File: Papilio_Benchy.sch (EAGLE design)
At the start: 133 parts, among them IC1 FT2232H, J1 USB MICRO, J4 HDMI-TYPE-A-RECEPTICALFCI1002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, SW1 SWITCH-2CH-6P-3010010P1, SW2 EVQQ2, T1 MOSFET-NCHANNELSMD, U1 ATMEGA32U4-XUMU, U11 PCA9306, U2 LTC3419EMS, U3 93C46B, U5 ARDUINO_MEGA_SHIELD, X2 12MHz, Y1 16MHz KX-7

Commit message: Power Supply PAR'd
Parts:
- removed PWR: (no value), led:LEDCHIP-LED0805
- removed R5: 1K8, GadgetFactory:R0805
- added PWRSELECT: (no value), jumper:JP2E
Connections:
- removed net 5V: C49.2, CONN1USB.VUSB, R11.2, R32A.2, U2.MODE, U2.RUN1, U2.VIN
- removed net N$1: PWR.A, R5A.1
- new net VBUS_A: CONN1USB.VUSB, PWRSELECT.1
- net 5V0: now also C49.2, PWRSELECT.2, R11.2, R32A.2, U2.MODE, U2.RUN1, U2.VIN; no longer R5A.2
- net GND: no longer PWR.C
- net VI: now also PWRSELECT.3
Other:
- moved on the sheet: S6BNA, S6BVCCAUX, S6BVCCINT

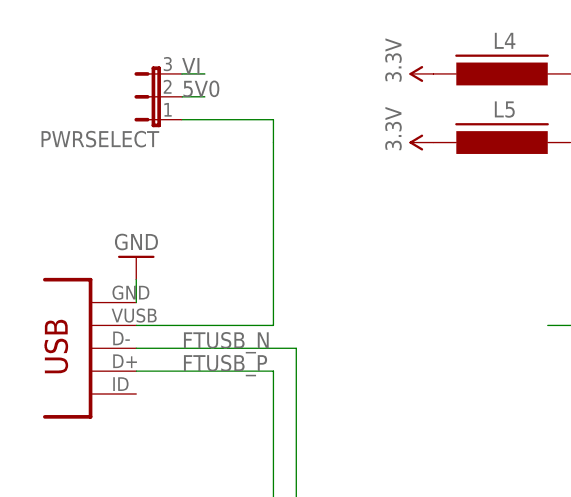
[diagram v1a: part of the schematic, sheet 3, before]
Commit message: SRAM Cleaned up
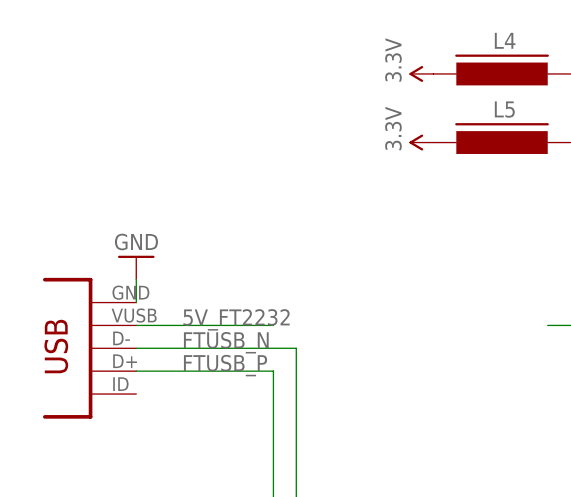
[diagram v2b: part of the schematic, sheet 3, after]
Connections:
- net VBUS_A renamed 5V_FT2232
- net XUSB renamed 5V_ARDUINO
- net 5V0: now also PWRIN.1
- net VI: no longer PWRIN.1
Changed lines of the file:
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@@
 </instance>
 <instance part="PWRIN" gate="A" x="193.04" y="444.5" rot="R270"/>
+<instance part="PWRSELECT" gate="1" x="162.56" y="472.44" rot="R90"/>
 </instances>
 <busses>
@@
 <pinref part="R32" gate="A" pin="2"/>
 </segment>
-</net>
-<net name="VI" class="0">
+<segment>
+<wire x1="165.1" y1="472.44" x2="167.64" y2="472.44" width="0.2032" layer="91"/>
+<label x="165.1" y="472.44" size="1.778" layer="95"/>
+<pinref part="PWRSELECT" gate="1" pin="2"/>
+</segment>
 <segment>
 <wire x1="170.18" y1="444.5" x2="190.5" y2="444.5" width="0.2032" layer="91"/>
 <label x="172.72" y="444.5" size="1.778" layer="95"/>
 <pinref part="PWRIN" gate="A" pin="1"/>
+</segment>
+</net>
+<net name="VI" class="0">
+<segment>
+<wire x1="165.1" y1="474.98" x2="167.64" y2="474.98" width="0.2032" layer="91"/>
+<label x="165.1" y="474.98" size="1.778" layer="95"/>
+<pinref part="PWRSELECT" gate="1" pin="3"/>
 </segment>
 </net>
@@
 <pinref part="R32" gate="A" pin="1"/>
 <pinref part="PWR1" gate="G$1" pin="A"/>
+</segment>
+</net>
+<net name="5V_FT2232" class="0">
+<segment>
+<wire x1="165.1" y1="469.9" x2="175.26" y2="469.9" width="0.2032" layer="91"/>
+<pinref part="PWRSELECT" gate="1" pin="1"/>
 </segment>
 </net>
@@
 <instance part="CONN1" gate="USB" x="12.7" y="142.24"/>
 <instance part="U3" gate="1" x="45.72" y="73.66" rot="MR0"/>
-<instance part="PWRSELECT" gate="1" x="20.32" y="170.18" rot="R90"/>
 </instances>
 <busses>
@@
 </segment>
 </net>
-<net name="VI" class="0">
-<segment>
-<wire x1="22.86" y1="172.72" x2="25.4" y2="172.72" width="0.2032" layer="91"/>
-<label x="22.86" y="172.72" size="1.778" layer="95"/>
-<pinref part="PWRSELECT" gate="1" pin="3"/>
-</segment>
-</net>
-<net name="VBUS_A" class="0">
-<segment>
-<wire x1="33.02" y1="154.94" x2="33.02" y2="144.78" width="0.2032" layer="91"/>
-<wire x1="33.02" y1="165.1" x2="33.02" y2="154.94" width="0.1524" layer="91"/>
-<wire x1="22.86" y1="167.64" x2="33.02" y2="167.64" width="0.2032" layer="91"/>
-<wire x1="33.02" y1="167.64" x2="33.02" y2="165.1" width="0.2032" layer="91"/>
-<pinref part="PWRSELECT" gate="1" pin="1"/>
+<net name="5V_FT2232" class="0">
+<segment>
 <pinref part="CONN1" gate="USB" pin="VUSB"/>
 <wire x1="17.78" y1="144.78" x2="33.02" y2="144.78" width="0.1524" layer="91"/>
-</segment>
-</net>
-<net name="5V0" class="0">
-<segment>
-<wire x1="22.86" y1="170.18" x2="25.4" y2="170.18" width="0.2032" layer="91"/>
-<label x="22.86" y="170.18" size="1.778" layer="95"/>
-<pinref part="PWRSELECT" gate="1" pin="2"/>
+<label x="22.86" y="144.78" size="1.778" layer="95"/>
 </segment>
 </net>
@@
 </segment>
 </net>
-<net name="XUSB" class="3">
-<segment>
-<wire x1="-81.28" y1="0" x2="-81.28" y2="10.16" width="0.1524" layer="91"/>
-<wire x1="-81.28" y1="10.16" x2="-66.04" y2="10.16" width="0.1524" layer="91"/>
+<net name="5V_ARDUINO" class="3">
+<segment>
 <wire x1="-101.6" y1="0" x2="-81.28" y2="0" width="0.1524" layer="91"/>
-<label x="-91.44" y="0" size="1.778" layer="95" rot="MR0"/>
-<label x="-78.74" y="10.16" size="1.778" layer="95"/>
+<label x="-81.28" y="0" size="1.778" layer="95" rot="MR0"/>
 <pinref part="J1" gate="G$1" pin="VBUS"/>
 </segment>

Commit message: Before connecting Avr JTAG
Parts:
- removed D2: CD1206-S01575, diode:DIODE-MINIMELF
- removed R47, R48, R49: 390, GadgetFactory:R0603
- removed R7: 10K, GadgetFactory_6.0:R0805
- C11, C3, C4, C5, C6, C7, C9: device SmartPrj:C-EUC0603 -> SmartPrj:C-EUC0603K
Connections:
- removed net +5V: C3.1, C4.1, D2.C, L6.1, R7A.2, RN2A.1, RN2C.1, RN2D.1, U1.UVCC, U1.VCC, U1.VCC1
- removed net N$10: R49A.2, U1.(SCLK/PCINT1)PB1
- removed net N$11: R48A.2, U1.(PDI/MOSI/PCINT2)PB2
- removed net N$12: R47A.2, U1.(PD0/MISO/PCINT3)PB3
- removed net VI: PWRSELECT.3
- net 5V0: now also C3.1, C4.1, L6.1, RN2A.1, RN2C.1, RN2D.1, U1.RESET, U1.UVCC, U1.VCC, U1.VCC1
- net 5V_ARDUINO: now also PWRSELECT.3
- net ARD_RESET: no longer D2.A, R7A.1, U1.RESET
- net MEGA_D40: no longer R47A.1
- net MEGA_D41: no longer R48A.1
- net MEGA_D42: no longer R49A.1

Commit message: Fully routed except for HDMI and AVR JTAG
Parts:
- removed LED1: (no value), led:LEDCHIPLED_0805
- removed ON: Green, led:LEDCHIPLED_0805
- removed R37: 390, GadgetFactory:R0805
- removed RN2: 1K, resistor-dil:4R-NCAY16
- removed RX, TX: Yellow, led:LEDCHIPLED_0805
- R2: value NM -> 10K; device SmartPrj:R-EU_R0402 -> GadgetFactory_6.0:R0603
- R3: value NM -> 1K; device SmartPrj:R-EU_R0402 -> GadgetFactory_6.0:R0603
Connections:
- net RD+ renamed AVRUSB_P
- net RD- renamed AVRUSB_N
- removed net ATMEGA_D2/SDA: R14A.2, U1.(SDA/INT1)PD1, U5.*D2
- removed net ATMEGA_D3/SCL: R15A.2, U1.(OC0B/SCL/INT0)PD0, U5.*D3
- removed net N$3: ON.A, RN2A.2
- removed net N$4: RN2C.2, TX.A
- removed net N$5: RN2D.2, RX.A
- removed net N$7: LED1.A, R37A.1
- removed net UGND: C7.2, R3.2, U1.UGND
- removed net VUSB: U1.VBUS
- new net ATMEGA_D2: R14A.2, U1.(PCINT5/OC1A/#OC4B/ADC12)PB5, U5.*D2
- new net ATMEGA_D3: R15A.2, U1.(ADC11/PCINT4)PB4, U5.*D3
- net 3V3: now also C3.1, C4.1, L6.1, R2A.2, U1.UVCC, U1.VCC, U1.VCC1
- net 5V0: no longer C3.1, C4.1, L6.1, RN2A.1, RN2C.1, RN2D.1, U1.RESET, U1.UVCC, U1.VCC, U1.VCC1
- net AGND: no longer C6.1, R2.1
- net ARD_RESET: now also R2A.1, U1.RESET
- net AREF: now also U5.AREF
- net ATMEGA_D4: now also U1.(T0/OC4D/ADC10)PD7; no longer U1.(OC3A/#0C4A)PC6
- net ATMEGA_D5*: now also U1.(T1/#OC4D/ADC9)PD6; no longer U1.(PCINT6/OC1B/OC4B/ADC13)PB6
- net ATMEGA_D6*: now also U1.(ICP1/ADC8)PD4; no longer U1.(PCINT5/OC1A/#OC4B/ADC12)PB5
- net ATMEGA_D7: now also U1.(SDA/INT1)PD1; no longer U1.(ADC11/PCINT4)PB4
- net ATMEGA_IO10*: now also U1.(PD0/MISO/PCINT3)PB3; no longer U1.(ICP1/ADC8)PD4
- net ATMEGA_IO11*: now also U1.(PDI/MOSI/PCINT2)PB2; no longer U1.(PCINT7/OC0A/OC1C/#RTS)PB7
- net ATMEGA_IO12: now also U1.(SCLK/PCINT1)PB1; no longer U1.(INT6/AIN0)PE6
- net ATMEGA_IO13*: now also R3A.2, U1.(INT6/AIN0)PE6; no longer RN2B.1, U1.(ICP3/CLK0/OC4A)PC7
- net ATMEGA_IO8: now also U1.(OC0B/SCL/INT0)PD0; no longer U1.(T0/OC4D/ADC10)PD7
- net ATMEGA_IO9*: now also U1.(PCINT7/OC0A/OC1C/#RTS)PB7; no longer U1.(T1/#OC4D/ADC9)PD6
- net ATMEGA_RXLED: no longer RX.C
- net ATMEGA_TXLED: no longer TX.C
- net GND: now also C6.1, C7.2, U1.UGND; no longer LED1.C, ON.C, R2.2, R3.1
- net MEGA_D14: now also U1.(PCINT6/OC1B/OC4B/ADC13)PB6
- net MEGA_D15: now also U1.(OC3A/#0C4A)PC6
- net MEGA_D16: now also U1.(ICP3/CLK0/OC4A)PC7
- net MEGA_D17: no longer R37A.2
- net N$2: now also R3A.1; no longer RN2B.2
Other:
- moved on the sheet: L

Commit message: Fully placed and routed! Needs verification and cleanup.
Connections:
- removed net ATMEGA_A2: U1.(ADC4/TCK)PF4, U5.A2
- removed net ATMEGA_A3: U1.(ADC5/TMS)PF5, U5.A3
- removed net ATMEGA_A4: U1.(ADC6/TDO)PF6, U5.A4
- removed net ATMEGA_A5: U1.(ADC7/TDI)PF7, U5.A5
- removed net MEGA_D28: S6B1.IO_L42P_GCLK7_1, U5.D28
- removed net MEGA_D30: S6B1.IO_L43P_GCLK5_1, U5.D30
- removed net MEGA_D32: S6B1.IO_L45P_1, U5.D32
- removed net MEGA_D34: S6B1.IO_L46P_1, U5.D34
- new net MEGA_D28/A5: S6B1.IO_L42P_GCLK7_1, U1.(ADC7/TDI)PF7, U5.A5, U5.D28
- new net MEGA_D30/A4: S6B1.IO_L43P_GCLK5_1, U1.(ADC6/TDO)PF6, U5.A4, U5.D30
- new net MEGA_D32/A3: S6B1.IO_L45P_1, U1.(ADC5/TMS)PF5, U5.A3, U5.D32
- new net MEGA_D34/A2: S6B1.IO_L46P_1, U1.(ADC4/TCK)PF4, U5.A2, U5.D34
- net MEGA_D49: now also J4.DATA0+; no longer J4.CLOCK+
- net MEGA_D50: now also J4.DATA0-; no longer J4.CLOCK-
- net MEGA_D51: now also J4.CLOCK+; no longer J4.DATA0+
- net MEGA_D52: now also J4.CLOCK-; no longer J4.DATA0-
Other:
- note removed: "TODO: Reset Line... Protect FPGA if 5V."
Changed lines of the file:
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@@
 <setting verticaltext="up"/>
 </settings>
-<grid distance="0.05" unitdist="inch" unit="inch" style="lines" multiple="1" display="no" altdistance="0.025" altunitdist="inch" altunit="inch"/>
+<grid distance="0.1" unitdist="inch" unit="inch" style="lines" multiple="1" display="no" altdistance="0.01" altunitdist="inch" altunit="inch"/>
 <layers>
 <layer number="1" name="Top" color="4" fill="1" visible="no" active="no"/>
@@
 </segment>
 </net>
-<net name="MEGA_D28" class="0">
+<net name="MEGA_D28/A5" class="0">
 <segment>
 <wire x1="10.16" y1="58.42" x2="-20.32" y2="58.42" width="0.1524" layer="91"/>
@@
 <pinref part="S6" gate="B1" pin="IO_L42P_GCLK7_1"/>
 </segment>
+<segment>
+<wire x1="-68.58" y1="124.46" x2="-45.72" y2="124.46" width="0.1524" layer="91"/>
+<label x="-63.5" y="124.46" size="1.778" layer="95"/>
+<pinref part="U5" gate="ARDUINO_MEGA" pin="A5"/>
+</segment>
 </net>
 <net name="MEGA_D29" class="0">
@@
 </segment>
 </net>
-<net name="MEGA_D30" class="0">
+<net name="MEGA_D30/A4" class="0">
 <segment>
 <wire x1="10.16" y1="53.34" x2="-20.32" y2="53.34" width="0.1524" layer="91"/>
@@
 <pinref part="S6" gate="B1" pin="IO_L43P_GCLK5_1"/>
 </segment>
+<segment>
+<wire x1="-68.58" y1="127" x2="-45.72" y2="127" width="0.1524" layer="91"/>
+<label x="-63.5" y="127" size="1.778" layer="95"/>
+<pinref part="U5" gate="ARDUINO_MEGA" pin="A4"/>
+</segment>
 </net>
 <net name="MEGA_D31" class="0">
@@
 </segment>
 </net>
-<net name="MEGA_D32" class="0">
+<net name="MEGA_D32/A3" class="0">
 <segment>
 <wire x1="10.16" y1="48.26" x2="-20.32" y2="48.26" width="0.1524" layer="91"/>
@@
 <pinref part="S6" gate="B1" pin="IO_L45P_1"/>
 </segment>
+<segment>
+<wire x1="-68.58" y1="129.54" x2="-45.72" y2="129.54" width="0.1524" layer="91"/>
+<label x="-63.5" y="129.54" size="1.778" layer="95"/>
+<pinref part="U5" gate="ARDUINO_MEGA" pin="A3"/>
+</segment>
 </net>
 <net name="MEGA_D33" class="0">
@@
 </segment>
 </net>
-<net name="MEGA_D34" class="0">
+<net name="MEGA_D34/A2" class="0">
 <segment>
 <wire x1="10.16" y1="43.18" x2="-20.32" y2="43.18" width="0.1524" layer="91"/>
@@
 <pinref part="S6" gate="B1" pin="IO_L46P_1"/>
 </segment>
+<segment>
+<wire x1="-68.58" y1="132.08" x2="-45.72" y2="132.08" width="0.1524" layer="91"/>
+<label x="-63.5" y="132.08" size="1.778" layer="95"/>
+<pinref part="U5" gate="ARDUINO_MEGA" pin="A2"/>
+</segment>
 </net>
 <net name="MEGA_D35" class="0">
@@
 </segment>
 </net>
-<net name="ATMEGA_A5" class="0">
-<segment>
-<wire x1="-68.58" y1="124.46" x2="-45.72" y2="124.46" width="0.1524" layer="91"/>
-<label x="-63.5" y="124.46" size="1.778" layer="95"/>
-<pinref part="U5" gate="ARDUINO_MEGA" pin="A5"/>
-</segment>
-</net>
-<net name="ATMEGA_A4" class="0">
-<segment>
-<wire x1="-68.58" y1="127" x2="-45.72" y2="127" width="0.1524" layer="91"/>
-<label x="-63.5" y="127" size="1.778" layer="95"/>
-<pinref part="U5" gate="ARDUINO_MEGA" pin="A4"/>
-</segment>
-</net>
-<net name="ATMEGA_A3" class="0">
-<segment>
-<wire x1="-68.58" y1="129.54" x2="-45.72" y2="129.54" width="0.1524" layer="91"/>
-<label x="-63.5" y="129.54" size="1.778" layer="95"/>
-<pinref part="U5" gate="ARDUINO_MEGA" pin="A3"/>
-</segment>
-</net>
-<net name="ATMEGA_A2" class="0">
-<segment>
-<wire x1="-68.58" y1="132.08" x2="-45.72" y2="132.08" width="0.1524" layer="91"/>
-<label x="-63.5" y="132.08" size="1.778" layer="95"/>
-<pinref part="U5" gate="ARDUINO_MEGA" pin="A2"/>
-</segment>
-</net>
 <net name="ATMEGA_A1" class="0">
 <segment>
@@
 <plain>
 <text x="-99.06" y="15.24" size="3.81" layer="94" ratio="10" rot="MR0">USB</text>
-<text x="-13.97" y="156.21" size="1.778" layer="91">TODO: Reset Line... Protect FPGA if 5V.</text>
 </plain>
 <instances>
@@
 </segment>
 </net>
-<net name="ATMEGA_A2" class="0">
+<net name="MEGA_D34/A2" class="0">
 <segment>
 <wire x1="53.34" y1="55.88" x2="71.12" y2="55.88" width="0.1524" layer="91"/>
@@
 </segment>
 </net>
-<net name="ATMEGA_A3" class="0">
+<net name="MEGA_D32/A3" class="0">
 <segment>
 <wire x1="53.34" y1="58.42" x2="71.12" y2="58.42" width="0.1524" layer="91"/>
@@
 </segment>
 </net>
-<net name="ATMEGA_A4" class="0">
+<net name="MEGA_D30/A4" class="0">
 <segment>
 <wire x1="53.34" y1="60.96" x2="71.12" y2="60.96" width="0.1524" layer="91"/>
@@
 </segment>
 </net>
-<net name="ATMEGA_A5" class="0">
+<net name="MEGA_D28/A5" class="0">
 <segment>
 <wire x1="53.34" y1="63.5" x2="71.12" y2="63.5" width="0.1524" layer="91"/>
@@
 </segment>
 </net>
-<net name="MEGA_D51" class="0">
+<net name="MEGA_D49" class="0">
 <segment>
 <wire x1="190.5" y1="137.16" x2="40.64" y2="137.16" width="0.2032" layer="91"/>
@@
 </segment>
 </net>
-<net name="MEGA_D52" class="0">
+<net name="MEGA_D50" class="0">
 <segment>
 <wire x1="190.5" y1="127" x2="40.64" y2="127" width="0.2032" layer="91"/>
@@
 </segment>
 </net>
-<net name="MEGA_D49" class="0">
-<segment>
-<wire x1="190.5" y1="121.92" x2="40.64" y2="121.92" width="0.2032" layer="91"/>
-<label x="40.64" y="121.92" size="1.778" layer="95"/>
-<pinref part="J4" gate="G$1" pin="CLOCK+"/>
-</segment>
-</net>
-<net name="MEGA_D50" class="0">
-<segment>
-<wire x1="190.5" y1="111.76" x2="40.64" y2="111.76" width="0.2032" layer="91"/>
-<label x="40.64" y="111.76" size="1.778" layer="95"/>
-<pinref part="J4" gate="G$1" pin="CLOCK-"/>
-</segment>
-</net>
 <net name="MEGA_D53" class="0">
 <segment>
@@
 </segment>
 </net>
+<net name="MEGA_D51" class="0">
+<segment>
+<wire x1="190.5" y1="121.92" x2="40.64" y2="121.92" width="0.2032" layer="91"/>
+<label x="40.64" y="121.92" size="1.778" layer="95"/>
+<pinref part="J4" gate="G$1" pin="CLOCK+"/>
+</segment>
+</net>
+<net name="MEGA_D52" class="0">
+<segment>
+<wire x1="190.5" y1="111.76" x2="40.64" y2="111.76" width="0.2032" layer="91"/>
+<label x="40.64" y="111.76" size="1.778" layer="95"/>
+<pinref part="J4" gate="G$1" pin="CLOCK-"/>
+</segment>
+</net>

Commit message: Silkscreen cleaned up.
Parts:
- removed C35, C36, C37, C38, C39, C40, C41: 0.1uF, dp_devices:CAPC603
- removed C48, C50: 22u/6V3, Bogdan_Commons:C0805
- removed C49: 10u/10V, Bogdan_Commons:C0805
- removed L5: (no value), dp_devices:FERRITE_BEAD603
- removed R33: 47K, GadgetFactory:R0805
- removed R34, R36, R38, R39: 10k, dp_devices:RESISTORR603
- removed R35: 2.2k, dp_devices:RESISTORR603
- removed R40, R41: 470, dp_devices:RESISTORR603
- removed U$9: POWER_ONLYNOTEXT, Papilio:POWER_ONLYNOTEXT
- removed U5: ARDUINO_MEGA_SHIELD, GadgetFactory_tmp:ARDUINO_MEGA_SHIELD
- added C100: 1uF, saanlima:C0402
- added C101, C102, C105: 100n, SmartPrj:C-EUC0603K
- added C103, C104: 1uF, SmartPrj:C-EUC0603K
- added C106, C107: 22p, SmartPrj:C-EUC0603K
- added C12, C13: .1uF, GadgetFactory:C0603
- added L1: 3.3uH, Bogdan_Commons:L_VLS3015
- added R100: 10K, saanlima:R0402
- added R102: 0, saanlima:R0402
- added R106, R107: 1K, saanlima:R0402
- added R109: 1M, SmartPrj:R-EU_R0603
- added R110: 10K, GadgetFactory_6.0:R0603
- added R5: 1K5 1%, Bogdan_Commons:R-SMALL0603
- added R7: 1K, GadgetFactory_6.0:R0603
- added U$4: POWER_ONLYNOTEXT, Papilio:POWER_ONLYNOTEXT
- added U101: ATMEGA32U4-XUMU, SmartPrj:ATMEGA32U4-XUMU
- C1: value 3.3uF -> 22u/6V3; device dp_devices:CAP_POLSMC_A -> Bogdan_Commons:C0805
- C10: value 27pF -> .1uF; device dp_devices:CAPC603 -> GadgetFactory:C0603
- C11: value 22p -> .1uF; device SmartPrj:C-EUC0603K -> GadgetFactory:C0603
- C15, C16, C17, C18, C27, C29, C30, C31: value .1uF -> 0.1uF; device GadgetFactory:C0603 -> dp_devices:CAPC603
- C19: value .1uF -> 3.3uF; device GadgetFactory:C0603 -> dp_devices:CAP_POLSMC_A
- C2: value 0.1uF -> 22u/6V3; device dp_devices:CAPC603 -> Bogdan_Commons:C0805
- C20: value 1uF -> 0.1uF; device saanlima:C0402 -> dp_devices:CAPC603
- C28: value .1uF -> 4.7uF; device GadgetFactory:C0603 -> dp_devices:CAP_POLSMC_A
- C3: value 100n -> 10u/10V; device SmartPrj:C-EUC0603K -> Bogdan_Commons:C0805
- C32: value 4.7uF -> .1uF; device dp_devices:CAP_POLSMC_A -> GadgetFactory:C0603
- C33: value 0.1uF -> .1uF; device dp_devices:CAPC603 -> GadgetFactory:C0603
- C4, C6: value 100n -> .1uF; device SmartPrj:C-EUC0603K -> GadgetFactory:C0603
- C5, C7: value 1uF -> .1uF; device SmartPrj:C-EUC0603K -> GadgetFactory:C0603
- C9: value 22p -> 27pF; device SmartPrj:C-EUC0603K -> dp_devices:CAPC603
- L3: value 3.3uH -> (none); device Bogdan_Commons:L_VLS3015 -> dp_devices:FERRITE_BEAD603
- R1: value 1M -> 22R; device SmartPrj:R-EU_R0603 -> GadgetFactory_6.0:R0805
- R10: value 10K -> 390; device saanlima:R0402 -> GadgetFactory:R0603
- R11: value 0 -> 390; device saanlima:R0402 -> GadgetFactory:R0603
- R12, R13: value 1K -> 390; device saanlima:R0402 -> GadgetFactory:R0603
- R2: value 10K -> 6K8 1%; device GadgetFactory_6.0:R0603 -> Bogdan_Commons:R-SMALL0603
- R22: value 390 -> 22R; device GadgetFactory:R0603 -> GadgetFactory_6.0:R0805
- R23, R24, R26: value 390 -> 10k; device GadgetFactory:R0603 -> dp_devices:RESISTORR603
- R25: value 390 -> 2.2k; device GadgetFactory:R0603 -> dp_devices:RESISTORR603
- R27: value 390 -> 12k 1%; device GadgetFactory:R0603 -> dp_devices:RESISTORR603
- R28: value 6K8 1% -> 10k; device Bogdan_Commons:R-SMALL0603 -> dp_devices:RESISTORR603
- R29, R30: value 1K5 1% -> 470; device Bogdan_Commons:R-SMALL0603 -> dp_devices:RESISTORR603
- R3: value 1K -> 1K5 1%; device GadgetFactory_6.0:R0603 -> Bogdan_Commons:R-SMALL0603
- R31: value 1K5 1% -> 47K; device Bogdan_Commons:R-SMALL0603 -> GadgetFactory:R0805
- R32: value 1K8 -> 4.7K; device GadgetFactory:R0805 -> GadgetFactory:R0603
- R4: value 22R -> 1K5 1%; device GadgetFactory_6.0:R0805 -> Bogdan_Commons:R-SMALL0603
- R6: value 22R -> 1K8; device GadgetFactory_6.0:R0805 -> GadgetFactory:R0603
- R8: value 4.7K -> 390
- R9: value 12k 1% -> 390; device dp_devices:RESISTORR603 -> GadgetFactory:R0603
- U$1: value POWER_ONLYNOTEXT -> JTAG_XILINX; device Papilio:POWER_ONLYNOTEXT -> GadgetFactory:JTAG_XILINX
- U$2: value JTAG_XILINX -> POWER_ONLYNOTEXT; device GadgetFactory:JTAG_XILINX -> Papilio:POWER_ONLYNOTEXT
- U1: value ATMEGA32U4-XUMU -> ARDUINO_MEGA_SHIELD; device SmartPrj:ATMEGA32U4-XUMU -> GadgetFactory_tmp:ARDUINO_MEGA_SHIELD
- renumbered CONN1 to FPGAUSB, J1 to AVRUSB, J4 to HDMI, L to LED, L6 to L100, PWR1 to PWR, PWRSELECT to PWRSEL, R42 to R104, R43 to R103, R44 to R105, R45 to R101, R46 to R108, RX1 to RX, S6 to S1, T1 to T100, TX1 to TX, U$7 to U$3, U11 to U100, X2 to X1
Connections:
- net !RESET: now also R28.2; no longer R34.2
- net 1.8V: now also C16.1, C19.+, C27.1, C31.1; no longer C1.+, C35.1, C36.1, C37.1
- net 1V2: now also C10.1, C13.1, C2.2, C32.1, C7.1, L2.2, R5.2; no longer C15.1, C21.1, C26.1, C31.1, C50.2, L3.2, R30.2
- net 3V3: now also C1.2, C101.1, C105.1, C11.1, C12.1, C20.1, C21.1, C26.1, C33.1, C5.1, C6.1, L1.2, L3.2, R106.1, R107.1, R110A.2, R2.2, R23.2, R24.2, R26.2, R28.1, R31A.2, R32A.2, U$1.JTAG_REF, U$2.3V3@P3, U$4.3V3@P3, U1.3.3V, U1.3V3@1, U1.3V3@2, U1.3V3@3, U1.3V3@4, U101.UVCC, U101.VCC, U101.VCC1; no longer C16.1, C19.1, C2.1, C27.1, C28.1, C3.1, C38.1, C39.1, C40.1, C41.1, C48.2, L2.2, L5.2, R12.1, R13.1, R28.2, R2A.2, R33A.2, R34.1, R36.2, R38.2, R39.2, R8A.2, U$1.3V3@P3, U$2.JTAG_REF, U$9.3V3@P3, U1.UVCC, U1.VCC, U1.VCC1, U5.3.3V, U5.3V3@1, U5.3V3@2, U5.3V3@3, U5.3V3@4
- net 5V0: now also C3.2, R102.2, R6A.2, U$2.5V0@P4, U$4.5V0@P4, U1.5V@0; no longer C49.2, R11.2, R32A.2, U$1.5V0@P4, U$9.5V0@P4, U5.5V@0
- net AC3: now also R30.1; no longer R40.1
- net AC4: now also R29.1; no longer R41.1
- net AD0-JTAG_TCK: now also U$1.JTAG_TCK; no longer U$2.JTAG_TCK
- net AD1-JTAG_TDI: now also U$1.JTAG_TDI; no longer U$2.JTAG_TDI
- net AD2-JTAG_TDO: now also U$1.JTAG_TDO; no longer U$2.JTAG_TDO
- net AD3-JTAG_TMS: now also U$1.JTAG_TMS; no longer U$2.JTAG_TMS
- net AGND: now also U101.GND3; no longer U1.GND3
- net ARD_RESET: now also R110A.1, U101.RESET; no longer R2A.1, U1.RESET
- net AREF: now also C102.2, U101.AREF; no longer C6.2, U5.AREF
- net ATMEGA_A0: now also U1.A0, U101.(ADC0)PF0; no longer U1.(ADC0)PF0, U5.A0
- net ATMEGA_A1: now also U1.A1, U101.(ADC1)PF1; no longer U1.(ADC1)PF1, U5.A1
- net ATMEGA_D0/RX: now also R21A.2, U1.RX, U101.(RXD1/AIN1/INT2)PD2; no longer R27A.2, U1.(RXD1/AIN1/INT2)PD2, U5.RX
- net ATMEGA_D1/TX: now also R20A.2, U1.TX, U101.(TXD1/INT3)PD3; no longer R26A.2, U1.(TXD1/INT3)PD3, U5.TX
- net ATMEGA_D2: now also R19A.2, U1.*D2, U101.(PCINT5/OC1A/#OC4B/ADC12)PB5; no longer R14A.2, U1.(PCINT5/OC1A/#OC4B/ADC12)PB5, U5.*D2
- net ATMEGA_D3: now also R18A.2, U1.*D3, U101.(ADC11/PCINT4)PB4; no longer R15A.2, U1.(ADC11/PCINT4)PB4, U5.*D3
- net ATMEGA_D4: now also R17A.2, U1.D4, U101.(T0/OC4D/ADC10)PD7; no longer R16A.2, U1.(T0/OC4D/ADC10)PD7, U5.D4
- net ATMEGA_D5*: now also R16A.2, U1.D5, U101.(T1/#OC4D/ADC9)PD6; no longer R17A.2, U1.(T1/#OC4D/ADC9)PD6, U5.D5
- net ATMEGA_D6*: now also R15A.2, U1.D6, U101.(ICP1/ADC8)PD4; no longer R18A.2, U1.(ICP1/ADC8)PD4, U5.D6
- net ATMEGA_D7: now also R14A.2, U1.D7, U101.(SDA/INT1)PD1; no longer R19A.2, U1.(SDA/INT1)PD1, U5.D7
- net ATMEGA_IO10*: now also R11A.2, U1.D10, U101.(PD0/MISO/PCINT3)PB3; no longer R22A.2, U1.(PD0/MISO/PCINT3)PB3, U5.D10
- net ATMEGA_IO11*: now also R10A.2, U1.D11, U101.(PDI/MOSI/PCINT2)PB2; no longer R23A.2, U1.(PDI/MOSI/PCINT2)PB2, U5.D11
- net ATMEGA_IO12: now also R9A.2, U1.D12, U101.(SCLK/PCINT1)PB1; no longer R24A.2, U1.(SCLK/PCINT1)PB1, U5.D12
- net ATMEGA_IO13*: now also R7A.2, R8A.2, U1.D13, U101.(INT6/AIN0)PE6; no longer R25A.2, R3A.2, U1.(INT6/AIN0)PE6, U5.D13
- net ATMEGA_IO8: now also R13A.2, U1.D8, U101.(OC0B/SCL/INT0)PD0; no longer R20A.2, U1.(OC0B/SCL/INT0)PD0, U5.D8
- net ATMEGA_IO9*: now also R12A.2, U1.D9, U101.(PCINT7/OC0A/OC1C/#RTS)PB7; no longer R21A.2, U1.(PCINT7/OC0A/OC1C/#RTS)PB7, U5.D9
- net ATMEGA_RXLED: now also U101.(SS/PCINT0)PB0; no longer U1.(SS/PCINT0)PB0
- net ATMEGA_TXLED: now also U101.(XCK1/#CTS)PD5; no longer U1.(XCK1/#CTS)PD5
- net AVCC: now also C104.1, U101.AVCC, U101.AVCC1; no longer C5.1, U1.AVCC, U1.AVCC1
- net AVRUSB_N: now also R1A.2, U101.D-; no longer R4A.2, U1.D-
- net AVRUSB_P: now also R22A.2, U101.D+; no longer R6A.2, U1.D+
- net D+: now also R22A.1; no longer R6A.1
- net D-: now also R1A.1; no longer R4A.1
- net DETECT: now also R100.2; no longer R10.2
- net EECLK: now also R24.1; no longer R36.1
- net EECS: now also R23.1; no longer R39.1
- net EEDATA: now also R25.2; no longer R35.2
- net FB_1V2: now also R4.2, R5.1; no longer R30.1, R31.2
- net FB_3V3: now also R2.1, R3.2; no longer R28.1, R29.2
- net GND: now also C1.1, C100.2, C101.2, C102.1, C103.2, C104.2, C105.2, C106.1, C107.2, C12.2, C13.2, C19.-, C2.1, C28.-, C3.1, C32.2, C6.2, C9.2, R100.1, R27.1, R3.1, R4.1, U$1.JTAG_GND, U$2.GND@P1, U$4.GND@P1, U1.GND@0, U1.GND@1, U1.GND@2, U1.GND@3, U1.GND@4, U1.GND@5, U1.GND@6, U101.(#HWB)PE2, U101.GND, U101.GND1, U101.GND2, U101.PAD, U101.UGND; no longer C1.-, C19.2, C2.2, C28.2, C3.2, C32.-, C35.2, C36.2, C37.2, C38.2, C39.2, C40.2, C41.2, C48.1, C49.1, C50.1, C6.1, C9.1, R10.1, R29.1, R31.1, R9.1, U$1.GND@P1, U$2.JTAG_GND, U$9.GND@P1, U1.(#HWB)PE2, U1.GND, U1.GND1, U1.GND2, U1.PAD, U1.UGND, U5.GND@0, U5.GND@1, U5.GND@2, U5.GND@3, U5.GND@4, U5.GND@5, U5.GND@6
- net MEGA_D0: now also R21A.1; no longer R27A.1
- net MEGA_D1: now also R20A.1; no longer R26A.1
- net MEGA_D10: now also R11A.1; no longer R22A.1
- net MEGA_D11: now also R10A.1; no longer R23A.1
- net MEGA_D12: now also R9A.1; no longer R24A.1
- net MEGA_D13: now also R8A.1; no longer R25A.1
- net MEGA_D14: now also U1.D14, U101.(PCINT6/OC1B/OC4B/ADC13)PB6; no longer U1.(PCINT6/OC1B/OC4B/ADC13)PB6, U5.D14
- net MEGA_D15: now also U1.D15, U101.(OC3A/#0C4A)PC6; no longer U1.(OC3A/#0C4A)PC6, U5.D15
- net MEGA_D16: now also U1.D16, U101.(ICP3/CLK0/OC4A)PC7; no longer U1.(ICP3/CLK0/OC4A)PC7, U5.D16
- net MEGA_D17: now also U1.D17; no longer U5.D17
- net MEGA_D18: now also U1.*D18; no longer U5.*D18
- net MEGA_D19: now also U1.*D19; no longer U5.*D19
- net MEGA_D2: now also R19A.1; no longer R14A.1
- net MEGA_D20: now also U1.*D20; no longer U5.*D20
- net MEGA_D21: now also U1.*D21; no longer U5.*D21
- net MEGA_D22: now also U1.D22; no longer U5.D22
- net MEGA_D23: now also U1.D23; no longer U5.D23
- net MEGA_D24: now also U1.D24; no longer U5.D24
- net MEGA_D25: now also U1.D25; no longer U5.D25
- net MEGA_D26: now also U1.D26; no longer U5.D26
- net MEGA_D27: now also U1.D27; no longer U5.D27
- net MEGA_D28/A5: now also U1.A5, U1.D28, U101.(ADC7/TDI)PF7; no longer U1.(ADC7/TDI)PF7, U5.A5, U5.D28
- net MEGA_D29: now also U1.D29; no longer U5.D29
- net MEGA_D3: now also R18A.1; no longer R15A.1
- net MEGA_D30/A4: now also U1.A4, U1.D30, U101.(ADC6/TDO)PF6; no longer U1.(ADC6/TDO)PF6, U5.A4, U5.D30
- net MEGA_D31: now also U1.D31; no longer U5.D31
- net MEGA_D32/A3: now also U1.A3, U1.D32, U101.(ADC5/TMS)PF5; no longer U1.(ADC5/TMS)PF5, U5.A3, U5.D32
- net MEGA_D33: now also U1.D33; no longer U5.D33
- net MEGA_D34/A2: now also U1.A2, U1.D34, U101.(ADC4/TCK)PF4; no longer U1.(ADC4/TCK)PF4, U5.A2, U5.D34
- net MEGA_D35: now also U1.D35; no longer U5.D35
- net MEGA_D36: now also U1.D36; no longer U5.D36
- net MEGA_D37: now also U1.D37; no longer U5.D37
- net MEGA_D38: now also U1.D38; no longer U5.D38
- net MEGA_D39: now also U1.D39; no longer U5.D39
- net MEGA_D4: now also R17A.1; no longer R16A.1
- net MEGA_D40: now also U1.D40; no longer U5.D40
- net MEGA_D41: now also U1.D41; no longer U5.D41
- net MEGA_D42: now also U1.D42; no longer U5.D42
- net MEGA_D43: now also R106.2, U1.D43; no longer R13.2, U5.D43
- net MEGA_D44: now also R107.2, U1.D44; no longer R12.2, U5.D44
- net MEGA_D45: now also U1.D45; no longer U5.D45
- net MEGA_D46: now also U1.D46; no longer U5.D46
- net MEGA_D47: now also U1.D47; no longer U5.D47
- net MEGA_D48: now also U1.D48; no longer U5.D48
- net MEGA_D49: now also U1.D49; no longer U5.D49
- net MEGA_D5: now also R16A.1; no longer R17A.1
- net MEGA_D50: now also U1.D50; no longer U5.D50
- net MEGA_D51: now also U1.D51; no longer U5.D51
- net MEGA_D52: now also U1.D52; no longer U5.D52
- net MEGA_D53: now also R32A.1, U1.D53; no longer R8A.1, U5.D53
- net MEGA_D6: now also R15A.1; no longer R18A.1
- net MEGA_D7: now also R14A.1; no longer R19A.1
- net MEGA_D8: now also R13A.1; no longer R20A.1
- net MEGA_D9: now also R12A.1; no longer R21A.1
- net N$2: now also R7A.1; no longer R3A.1
- net N$22: now also C9.1; no longer C8.1
- net N$23: now also C8.1; no longer C10.1
- net N$24: now also R30.2; no longer R40.2
- net N$25: now also R29.2; no longer R41.2
- net N$45: now also R25.1, R26.1; no longer R35.1, R38.1
- net N$48: now also C14.+, C15.1, L3.1; no longer C32.+, C34.1, L5.1
- net N$49: now also C28.+, C34.1; no longer C14.+, C33.1
- net N$6: now also C100.1; no longer C20.1
- net N$8: now also R6A.1; no longer R32A.1
- net N$9: now also R27.2; no longer R9.2
- net RESET: now also R31A.1, U1.RES; no longer R33A.1, U5.RES
- net SW_1V2: now also L2.1; no longer L3.1
- net SW_3V3: now also L1.1; no longer L2.1
- net TX_HDMI_5V: now also R102.1; no longer R11.1
- net UCAP: now also C103.1, U101.UCAP; no longer C7.1, U1.UCAP
- net XTAL1: now also C107.1, R109.1, U101.XTAL1; no longer C11.1, R1.1, U1.XTAL1
- net XTAL2: now also C106.2, R109.2, U101.XTAL2; no longer C9.2, R1.2, U1.XTAL2
